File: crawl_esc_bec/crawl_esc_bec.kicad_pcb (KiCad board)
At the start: 2 copper layers, 28 x 32 mm, 42 parts, among them IC1 L78M06ABDT-TR, IC2 LM25085AMY, IC3 LMR62014XMFE/NOPB, Q2 SQJ461EP-T1-GE3

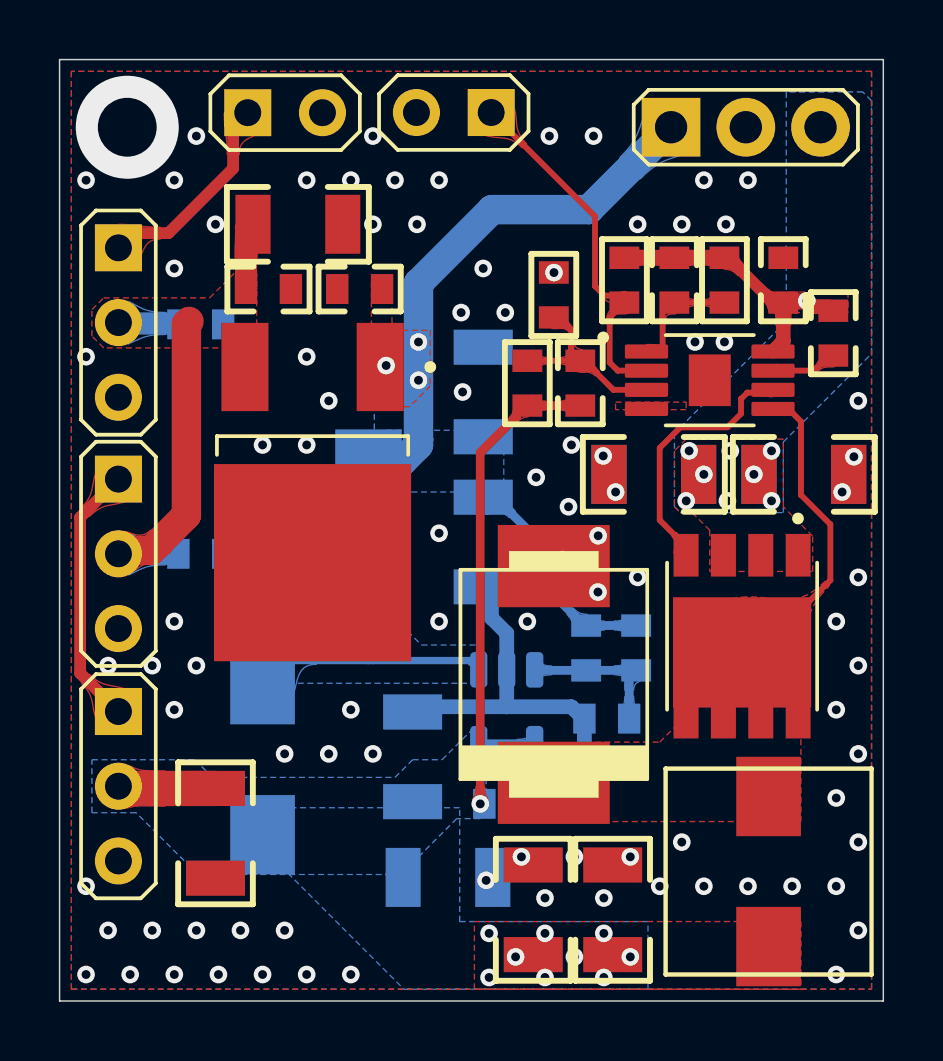
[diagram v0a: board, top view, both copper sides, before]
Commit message: change stepup isens layout
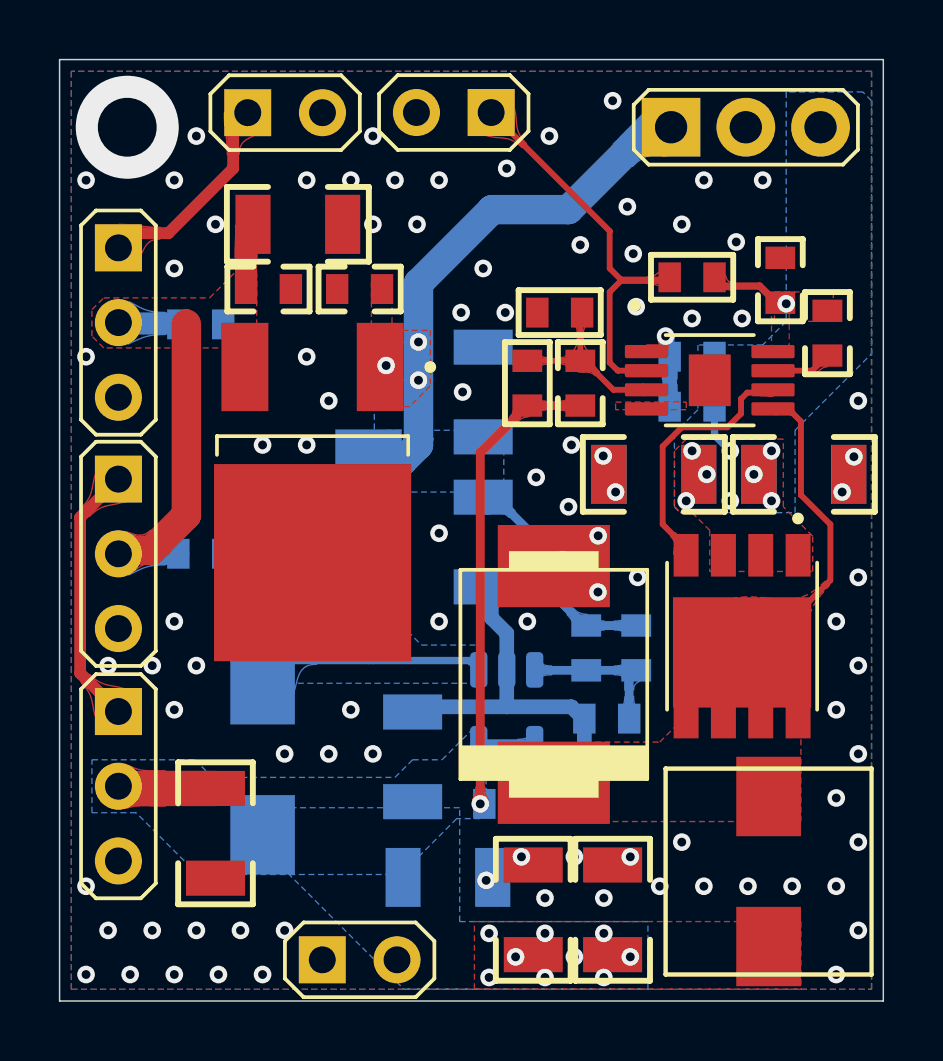
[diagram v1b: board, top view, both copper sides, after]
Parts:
- added ST7: ~, Super_Lib_V1_0.IntLib:STL2X1, F.Cu at (144.7, 119.6)
- C2, R1: moved to B.Cu
- moved R1 4.44 mm to (156.0, 100.8), turned to 0 degrees
- moved C2 2.67 mm to (156.0, 99.1), turned to 180 degrees
- moved R2 2.30 mm to (156.0, 96.4), turned to 180 degrees
- moved R4 0.63 mm to (151.5, 97.6), turned to 180 degrees
- moved C1 0.20 mm to (160.6, 98.3)
- moved C7 0.10 mm to (159.0, 96.5)
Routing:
- net VCC: track 9.75 -> 6.20 mm
- net /SHD: track 12.2 -> 13.5 mm
- net Net-(D1-PadK): track 12.0 -> 10.8 mm
- net Net-(C2-Pad2): track 4.08 -> 4.16 mm, vias 0 -> 1
- net GND: vias 90 -> 91
